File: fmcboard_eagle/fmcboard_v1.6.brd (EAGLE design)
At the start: 147 x 74 mm, 284 parts, among them IC1 OPA699ID, IC10 LM358, IC11 7805DT, IC12 SN74AUC2G66DCTR, IC13 SN74AUC2G66DCTR, IC14 SN74AUC2G66DCTR, IC15 SN74AUC2G66DCTR, IC16 DAC7578SPWR, IC17 SN74AUC2G66DCTR, IC18 SN74AUC2G66DCTR, IC19 SN74AUC2G66DCTR, IC2 DAC7578SPWR, IC20 SN74AUC2G66DCTR, IC21 74AUP2GU04GW, IC22 74AUP2GU04GW, IC23 74AUP2GU04GW, IC24 74AUP2GU04GW, IC25 MC7905ACD2TR4G, IC26 AMS1117-1.8, IC27 LM358, IC28 SN74AUC2G66DCTR, IC29 LM337KVURG3, IC3 LTC6229IMS8E#TRPBF, IC30 SN74AUC2G66DCTR, IC31 SN74AUC2G66DCTR, IC32 SN74AUC2G66DCTR, IC33 LTC6229IMS8E#TRPBF, IC34 74AUP2GU04GW, IC35 74AUP2GU04GW, IC4 OPA695IDR, IC5 LTC6229IMS8E#TRPBF, IC6 OPA695IDR, IC7 OPA699ID, IC8 LM358, IC9 LM358, J1 8pin, J12 4p-2.54, J13 4p-2.54, J2 ASP-134604-01, J3 4p-2.54, J4 4p-2.54, J5 4p-2.54, J6 4p-2.54, J7 4p-2.54, J8 4p-2.54

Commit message: Added extra 4 DAC outputs, 2 positive and 2 negative Move all to 0402 R and C Replace 100uF with 10 10uF Remove dacoffset variable resistor, replace with DAC N Set VH and VL to 1.8 and GND Copies of pulse out and amp out to sma - nah
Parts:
- removed C8: 0.1uF, rcl:C0402K
- added C116, C117: 100pF, rcl:C0402K
- added C4, C95: 0.1uF, rcl:C0402K
- moved R115 222.8 mm to (59.0, 39.0), turned to 180 degrees
- moved R17 216.1 mm to (59.0, 37.0), turned to 180 degrees
- moved R111 215.5 mm to (89.0, 34.0)
- moved R113 207.2 mm to (89.0, 32.0)
- moved R114 203.9 mm to (90.0, 18.0)
- moved R112 199.5 mm to (90.0, 20.0)
- moved IC34 196.8 mm to (90.0, 28.0)
- moved IC35 187.8 mm to (90.0, 15.0)
- moved IC33 173.2 mm to (97.0, 7.00)
- moved R108 171.2 mm to (102.0, 7.00), turned to 180 degrees
- moved R91 167.8 mm to (92.0, 3.00), turned to 180 degrees
- moved R105 164.1 mm to (102.0, 5.00), turned to 180 degrees
- moved R110 159.8 mm to (102.0, 3.00), turned to 180 degrees
- moved R107 158.4 mm to (102.0, 8.40), turned to 180 degrees
- moved IC31 157.9 mm to (97.0, 28.0)
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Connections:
- net 1V8-: now also C117.1, C95.1
- net GND: now also C116.2, C117.2, C4.2, C95.2; no longer C8.1, C8.2
- net VS+: now also C116.1, C4.1
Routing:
- net OPOUT_H10: track 0.79 -> 94.6 mm, vias 0 -> 2
- net PULSESUMIN: track 0.00 -> 90.7 mm
- net VIN+CLEAN: track 0.00 -> 44.3 mm
- net VIN-CLEAN: track 0.00 -> 27.2 mm
- net AR_5V: track 0.00 -> 27.0 mm
- net TRANSOUT: track 0.00 -> 25.8 mm
- net GND: track 20.2 -> 0.00 mm
- net N$10: track 0.00 -> 18.3 mm
- net OP2OUT: track 0.00 -> 18.1 mm
- net VIN+: track 0.00 -> 17.6 mm
- net OP1BUF: track 0.00 -> 16.6 mm
- net 1V8-: track 0.00 -> 15.2 mm
- net IO1: track 0.00 -> 15.1 mm
- net PULSESUMOUT: track 0.00 -> 11.6 mm
- net VIN-: track 0.00 -> 10.9 mm
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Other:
- board text removed: "C18"
- board text removed: "C19"
- board text removed: "C22"
- board text removed: "C23"
- board text removed: "DACOFFSET"
- board text removed: "DACP1 P2 P3 P4 DACN1 N2 N3 N4"
- board text removed: "OFFSETOUT"
- board text removed: "Offset"
- board text removed: "PULSEOFFSET_P,_NI"
- board text removed: "VH"
- board text removed: "VL"

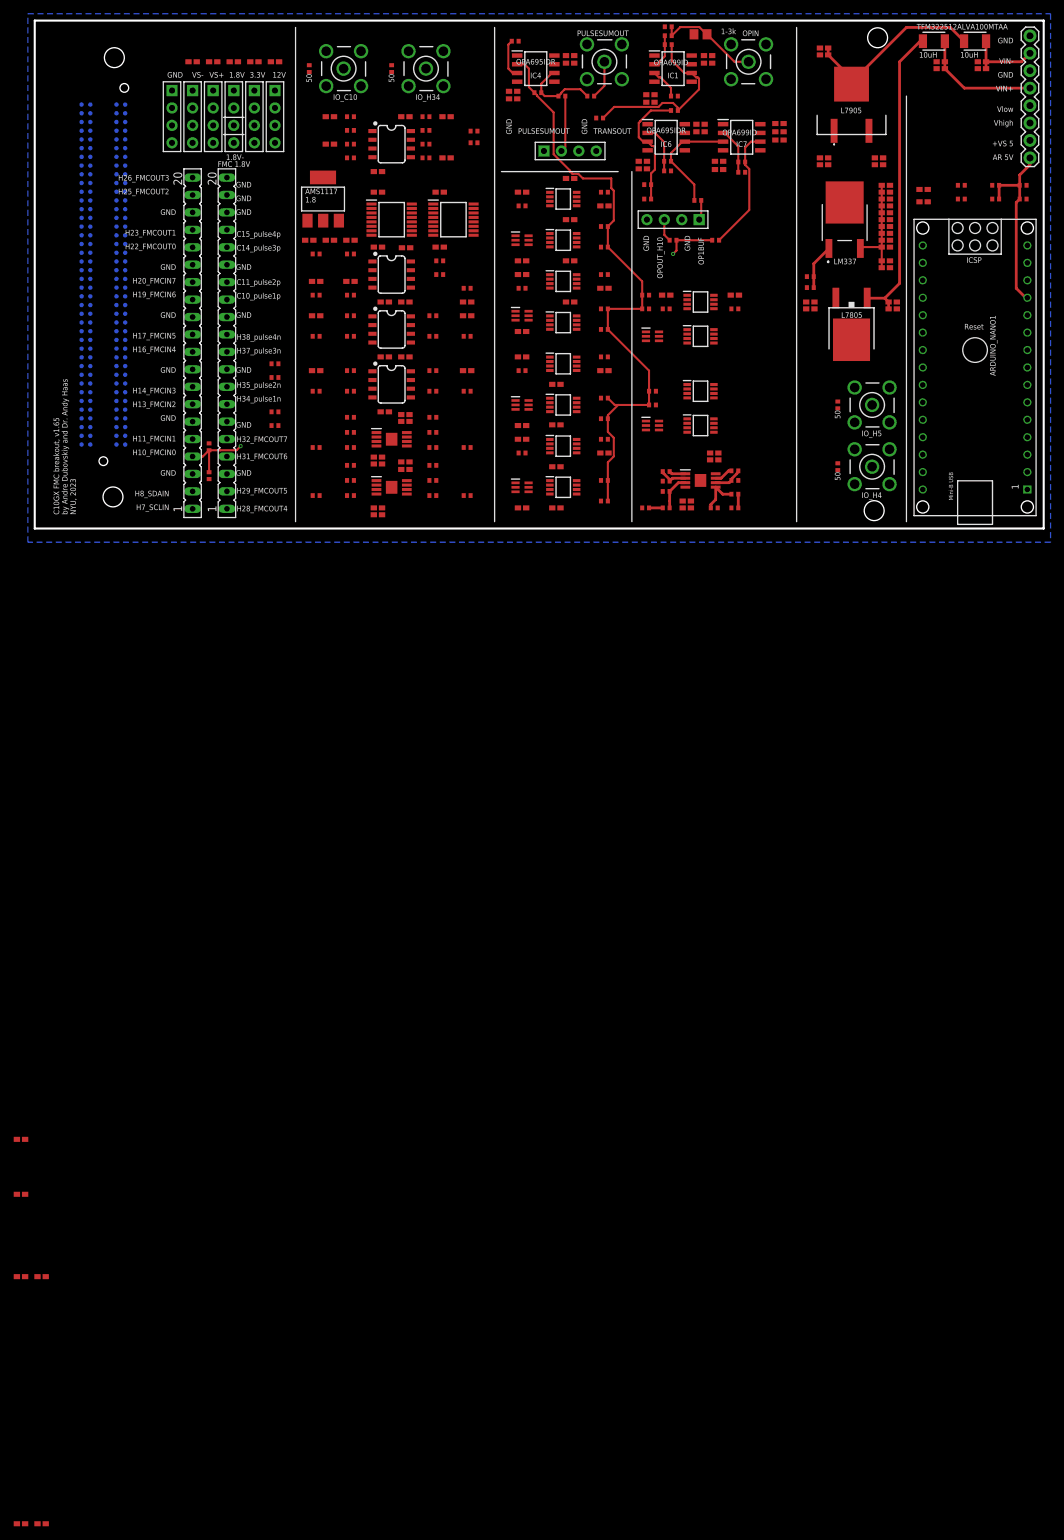
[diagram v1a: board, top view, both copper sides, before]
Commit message: power routed
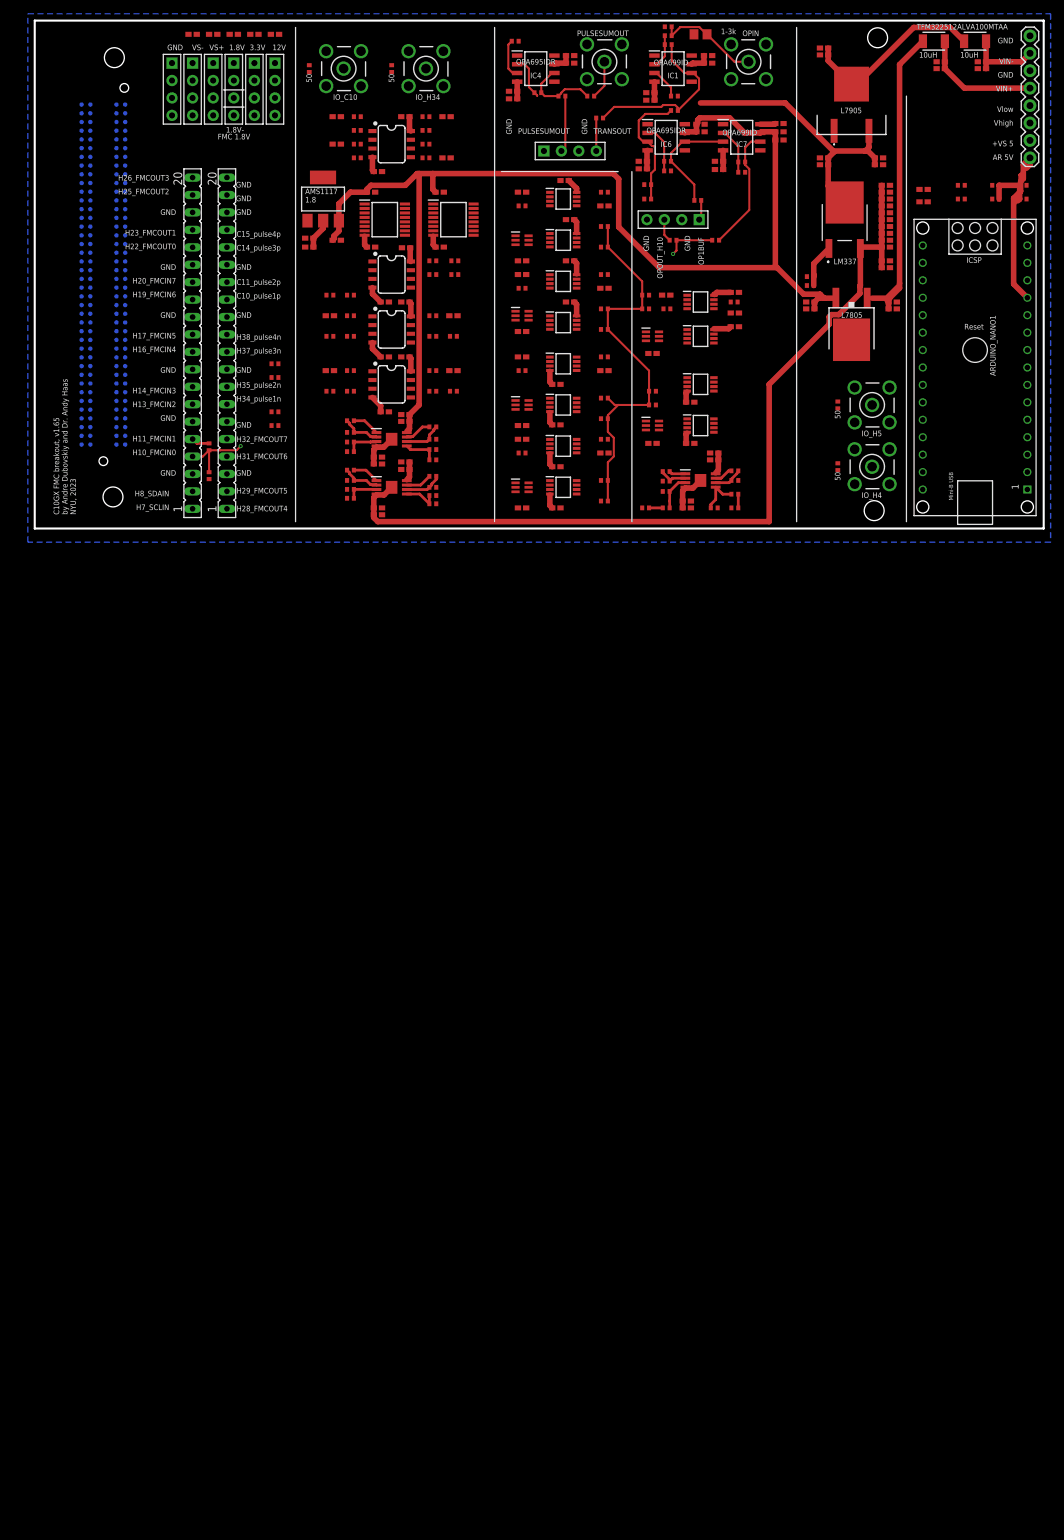
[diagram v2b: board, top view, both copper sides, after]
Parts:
- removed C11, C64, C80: 1uF, rcl:C0402K
- removed R60, R73, R84: 100, rcl:R0402
- moved C105 192.3 mm to (90.0, 25.5), turned to 180 degrees
- moved C104 185.2 mm to (95.5, 12.4)
- moved C103 171.3 mm to (102.0, 29.4)
- moved C102 167.6 mm to (102.0, 34.4)
- moved C30 152.3 mm to (90.0, 12.4)
- moved C101 145.1 mm to (95.5, 18.4)
- moved R79 19.4 mm to (61.2, 37.0)
- moved R85 19.1 mm to (61.2, 39.0)
- moved C3 6.08 mm to (44.0, 42.0)
- moved R27 5.31 mm to (58.0, 10.0)
- moved R21 5.04 mm to (46.0, 11.2)
- moved R37 5.02 mm to (46.0, 4.40)
- moved R44 5.00 mm to (58.0, 4.80)
- moved C10 4.00 mm to (23.0, 72.0)
- moved C12 4.00 mm to (35.0, 72.0)
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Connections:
- removed net N$29: IC16.4, R60.1
- removed net N$36: IC10.1, R35.2, R73.2
- removed net N$39: IC16.13, R84.2
- net 1V8: now also C55.1, IC16.8
- net DACOFFSET: now also IC16.4; no longer C64.2, R60.2
- net GND: no longer C11.1, C64.1, C80.2
- net PULSEOFFSET_NI: now also IC10.1, R35.2; no longer C11.2, R73.1
- net PULSEOFFSET_P: now also IC16.13; no longer C80.1, R84.1
- net VS+: no longer C55.1, IC16.8
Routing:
- net VS+: track 0.00 -> 191.7 mm
- net 1V8-: track 15.2 -> 159.3 mm
- net VS-: track 0.00 -> 62.2 mm
- net PULSESUMIN: track 90.7 -> 63.8 mm
- net 1V8: track 0.00 -> 23.4 mm
- net AR_5V: track 27.0 -> 49.5 mm
- net N$13: track 0.00 -> 5.68 mm
- net N$4: track 0.00 -> 5.64 mm
- net N$6: track 0.00 -> 5.48 mm
- net N$12: track 0.00 -> 5.44 mm
- net N$15: track 0.00 -> 5.08 mm
- net N$5: track 0.00 -> 5.01 mm
- net N$38: track 0.00 -> 4.80 mm
- net N$7: track 0.00 -> 4.72 mm
- net N$14: track 0.00 -> 4.60 mm
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
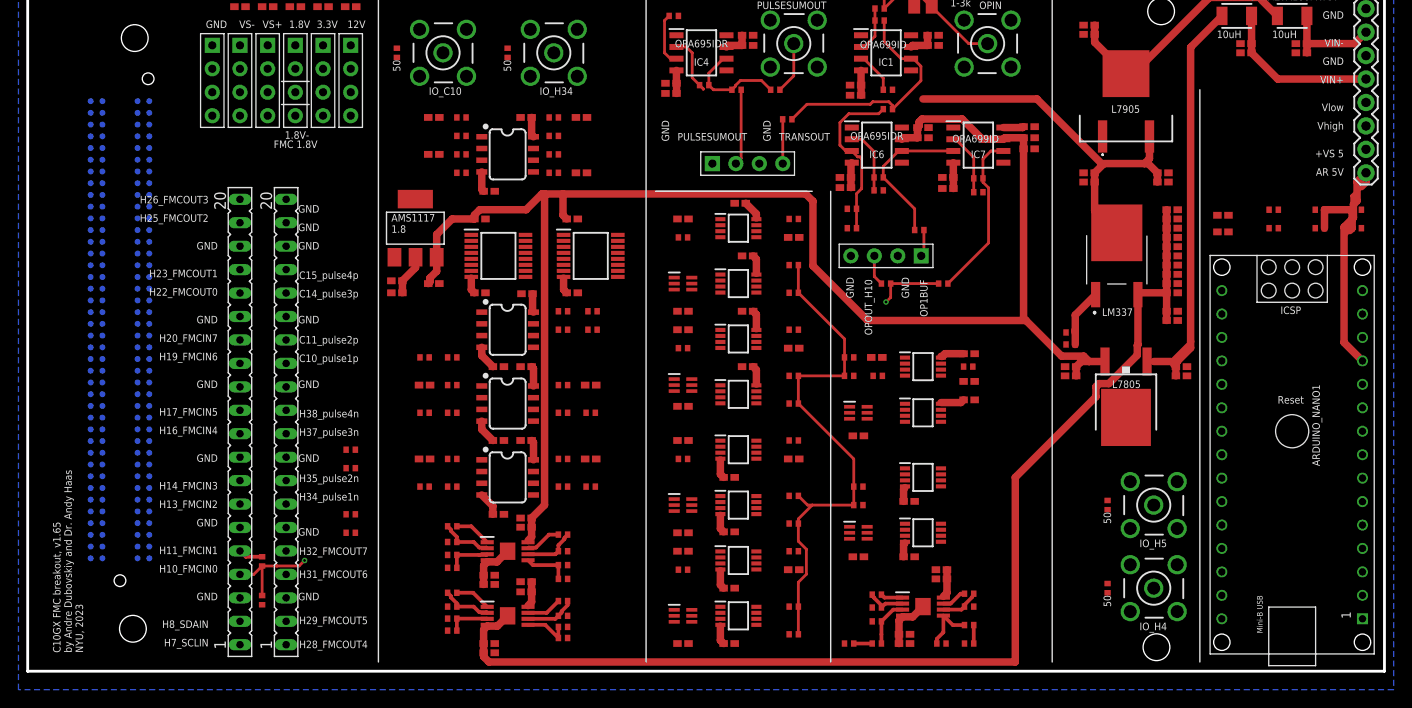
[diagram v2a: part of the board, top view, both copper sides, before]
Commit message: power routed
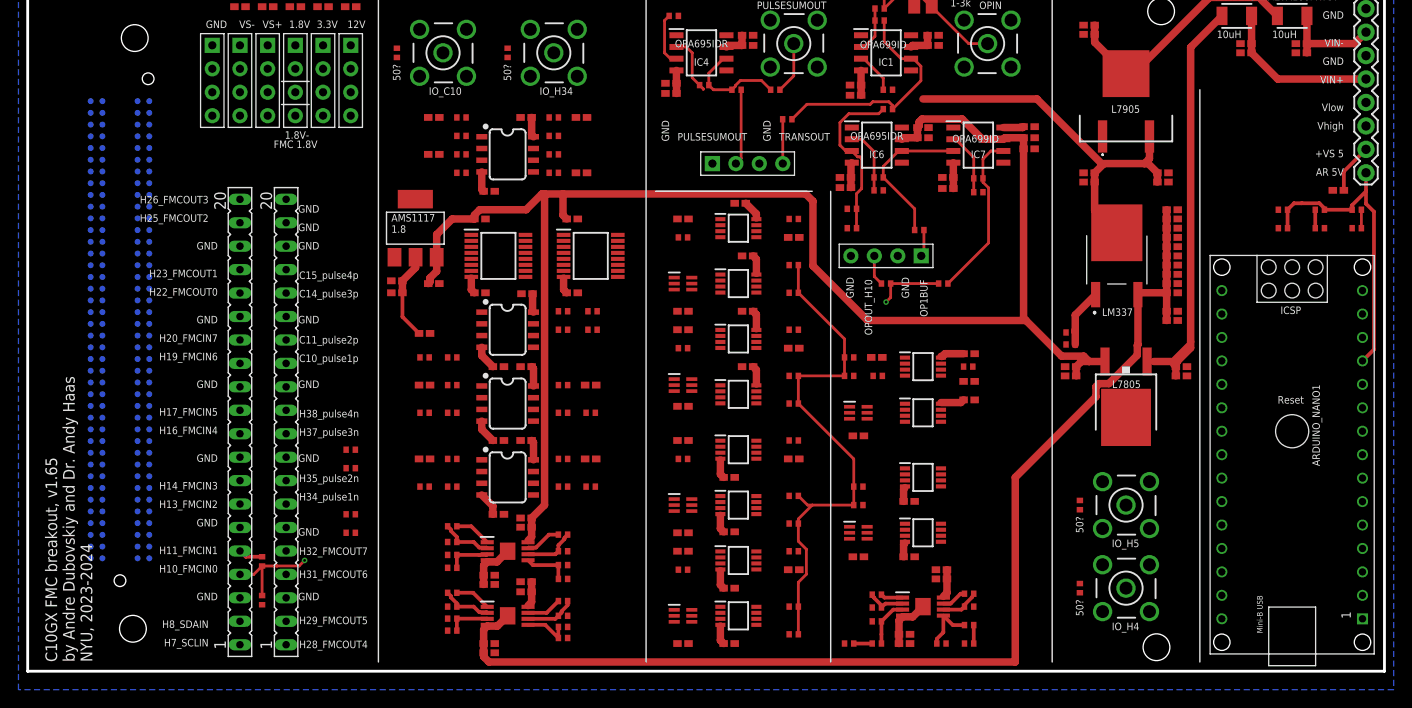
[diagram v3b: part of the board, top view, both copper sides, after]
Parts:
- R15, R16, R4, R5: value 50 -> 50?
- moved C36 87.4 mm to (43.0, 36.6)
- moved C6 13.3 mm to (142.0, 52.1), turned to 180 degrees
- moved R87 9.00 mm to (144.0, 48.0)
- moved R48 8.00 mm to (136.0, 48.0), turned to 180 degrees
- moved R90 5.39 mm to (140.0, 48.0), turned to 180 degrees
- moved R49 4.47 mm to (136.0, 50.0)
- moved IO_H4 3.00 mm to (119.0, 9.00)
- moved IO_H5 3.00 mm to (119.0, 18.0)
- moved R15 3.00 mm to (114.0, 9.00)
- moved R16 3.00 mm to (114.0, 18.0)
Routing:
- net AR_5V: track 49.5 -> 33.5 mm
- net 1V8: track 23.4 -> 29.6 mm
- net VS+: track 191.7 -> 197.1 mm
- net AR_SDAIN: track 0.00 -> 2.00 mm
- net AR_SCLIN: track 0.00 -> 2.00 mm
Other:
- board text added: "C10GX FMC breakout, v1.65 by Andre Dubovskiy and Dr. Andy Haas NYU, 2023-2024"
- board text removed: "C10GX FMC breakout, v1.65 by Andre Dubovskiy and Dr. Andy Haas NYU, 2023"

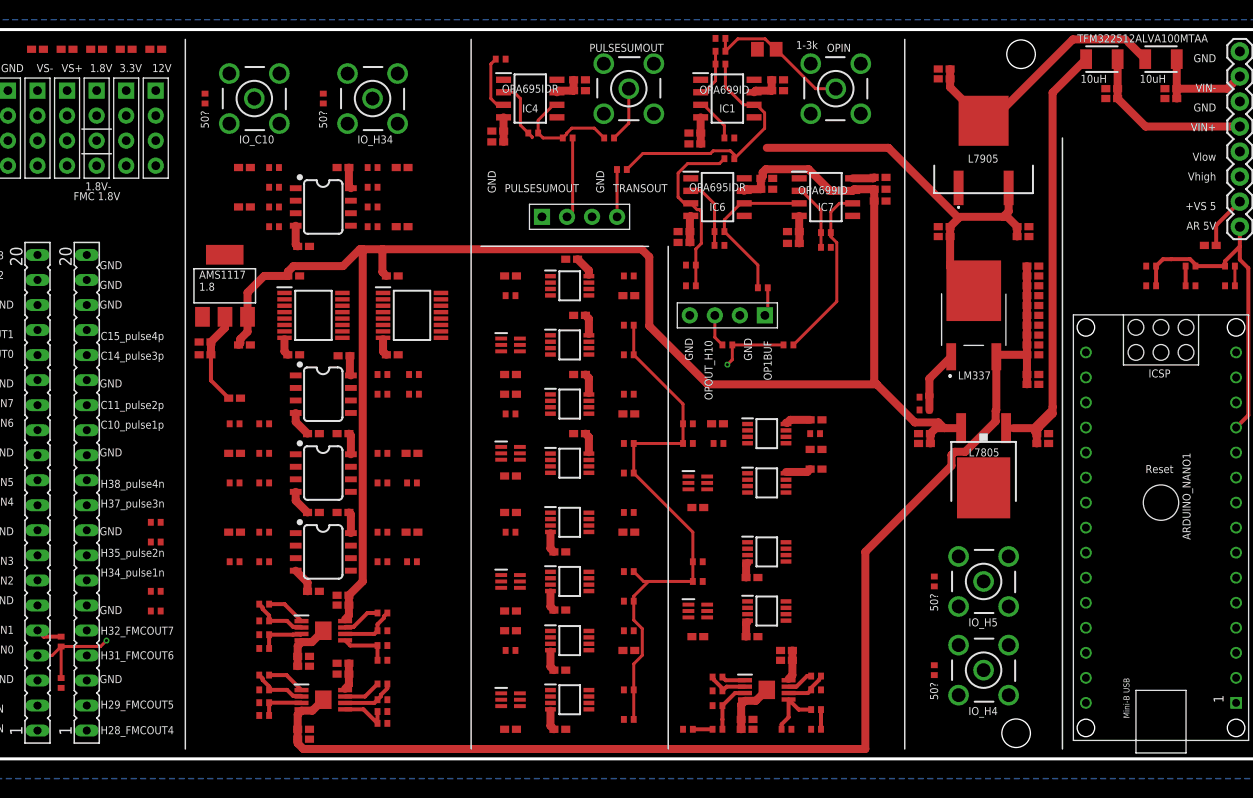
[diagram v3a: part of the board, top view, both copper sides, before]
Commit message: power routed, plus gnd
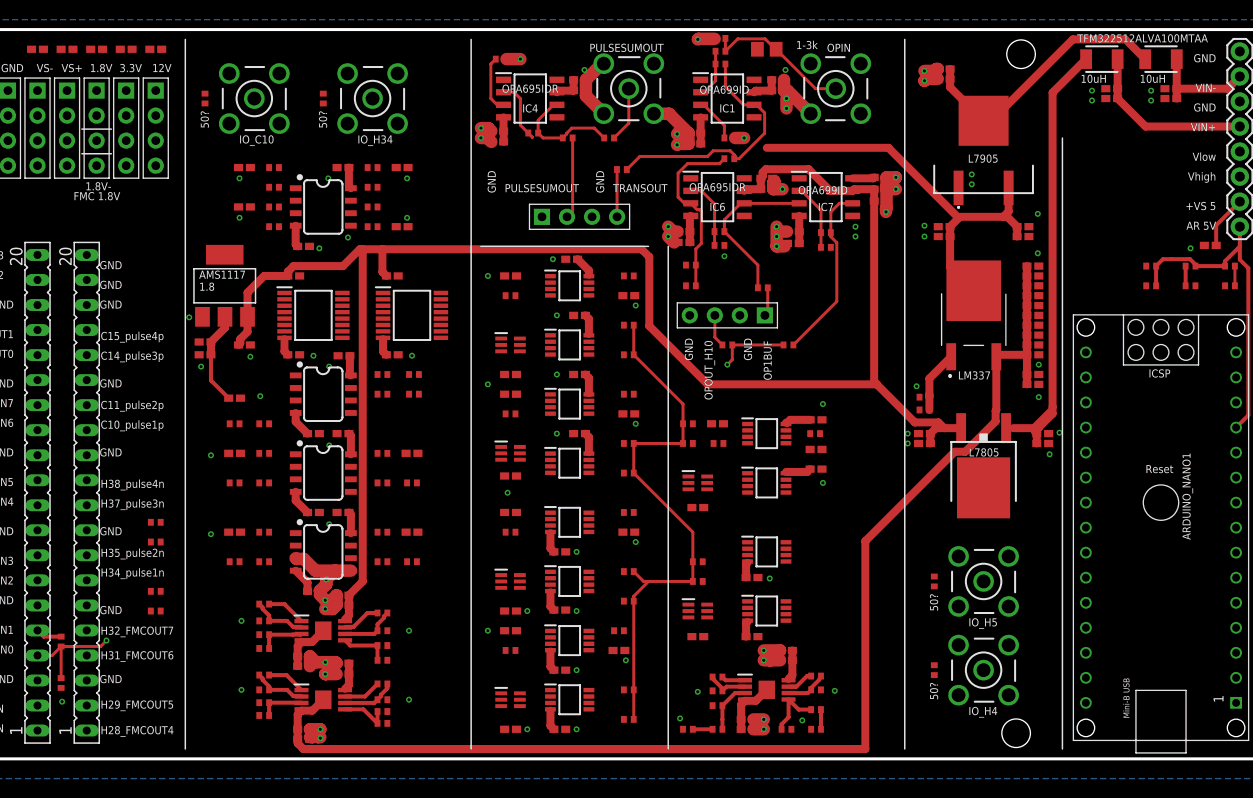
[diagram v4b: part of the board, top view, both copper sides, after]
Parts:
- moved C20 1.00 mm to (82.0, 11.0)
- moved R77 1.00 mm to (82.0, 13.0)
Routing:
- net GND: track 0.00 -> 76.3 mm, vias 0 -> 102
- net PULSESUMIN: track 63.8 -> 63.0 mm

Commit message: routed
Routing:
- net GND: track 76.3 -> 448.3 mm, vias 102 -> 114
- net C27: track 0.00 -> 205.8 mm, vias 0 -> 2
- net 1V8: track 29.6 -> 229.8 mm, vias 0 -> 8
- net C26: track 0.00 -> 196.2 mm, vias 0 -> 4
- net 1V8-: track 159.3 -> 353.9 mm, vias 0 -> 1
- net VS-: track 62.2 -> 254.8 mm, vias 0 -> 6
- net SCLIN: track 0.00 -> 180.7 mm, vias 0 -> 3
- net VS+: track 197.1 -> 376.9 mm, vias 0 -> 7
- net SDAIN: track 0.00 -> 176.2 mm, vias 0 -> 2
- net AR_SCLIN2: track 0.00 -> 161.9 mm, vias 0 -> 3
- net H34: track 0.00 -> 134.1 mm, vias 0 -> 2
- net AR_SDAIN2: track 0.00 -> 133.9 mm, vias 0 -> 5
- net H5: track 0.00 -> 133.7 mm, vias 0 -> 1
- net C23: track 2.00 -> 132.5 mm, vias 0 -> 3
- net C19: track 0.00 -> 129.6 mm, vias 0 -> 4
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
